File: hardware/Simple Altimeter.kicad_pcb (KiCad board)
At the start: 4 copper layers, 15.2 x 28.8 mm, 40 parts, among them J1 USB_C_Receptacle_USB2.0, J2 Conn_01x05_Pin, Q2 DMN3607LW, Q3 Q_NMOS_GDS, SW2 SW_Push, U1 WS4518, U2 BMP280, U3 W25Q16JVUXIQ, U4 STM32F042G6Ux, U5 XB6042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

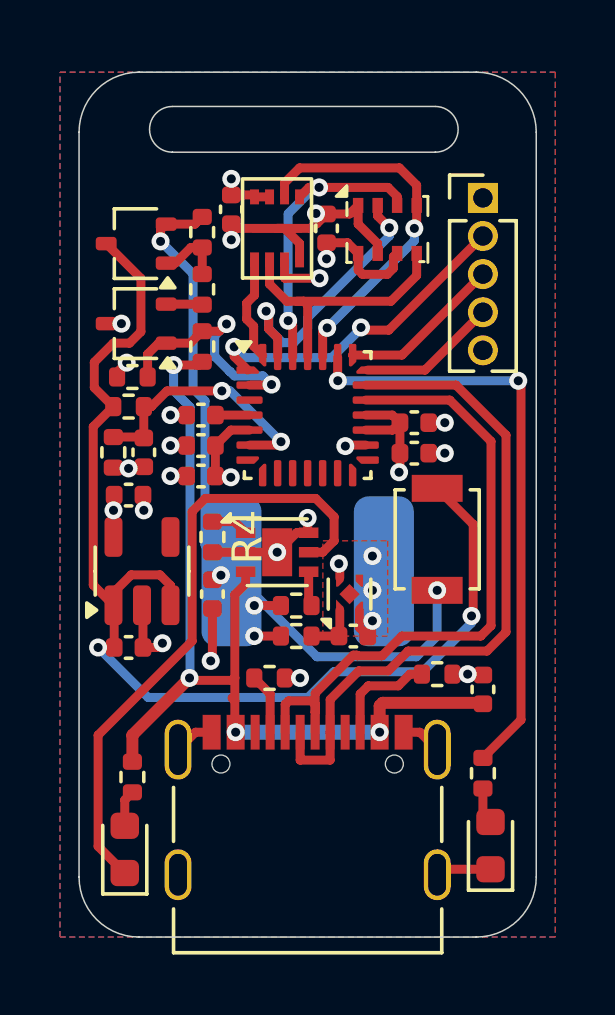
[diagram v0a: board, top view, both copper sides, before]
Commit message: Fixed boot pin and strengthened teather loop. Added BOMs and manufacturing data.
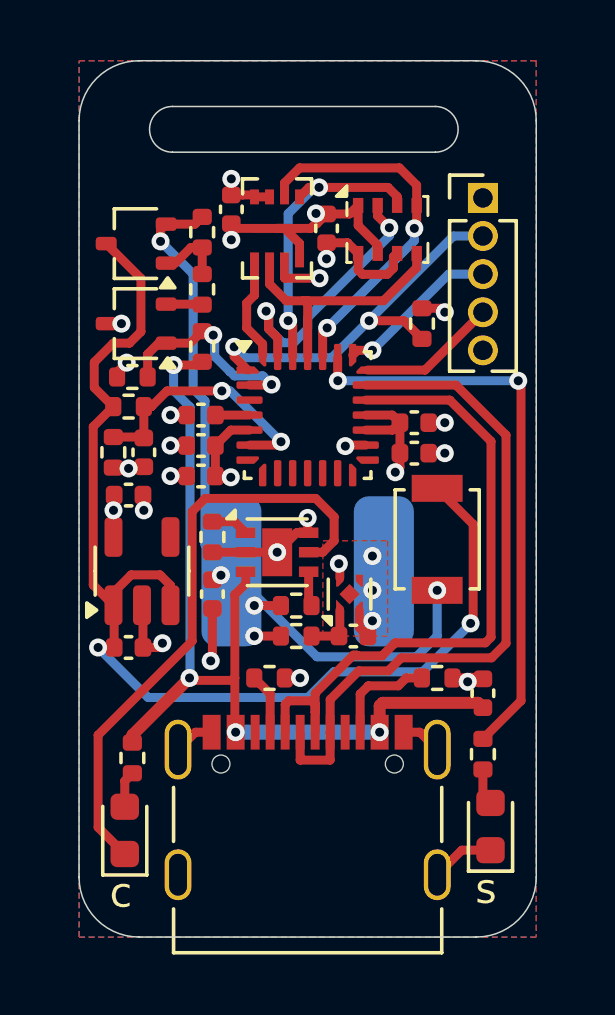
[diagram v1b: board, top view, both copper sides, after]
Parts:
- added R14: 33k3, Resistor_SMD:R_0402_1005Metric, F.Cu at (153.2, 105.8)
- D2: value LED -> RED LED
- moved R10 0.64 mm to (155.2, 120.1)
- moved D1 0.63 mm to (143.3, 122.7)
- moved D2 0.63 mm to (155.4, 122.6)
- moved R11 0.63 mm to (143.5, 120.3)
- moved R7 0.13 mm to (153.7, 117.6)
- moved C15 0.13 mm to (155.2, 118.1)
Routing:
- net /BATT-: track 3.78 -> 0.97 mm
- net /BOOT: track 11.2 -> 13.1 mm
- net /STAY_ALIVE: track 8.08 -> 7.07 mm
- net +5V: track 31.8 -> 30.8 mm
- net GND: track 28.9 -> 29.8 mm, vias 19 -> 20
- net Net-(D1-K): track 20.7 -> 20.1 mm
- net /LED: track 19.9 -> 19.3 mm
- net /SWDCLK: vias 0 -> 1
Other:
- board size 15.2 x 28.8 mm -> 15.2 x 29.2 mm
- board text added: "c"
- board text added: "s"

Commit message: Corrected Q1 schematic symbol (was NMOS, now correctly showing PMOS)
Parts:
- removed Q3: Q_NMOS_GDS, Package_TO_SOT_SMD:SOT-323_SC-70
- added Q1: DMP3099L, Package_TO_SOT_SMD:SOT-323_SC-70, F.Cu at (143.6, 103.1)
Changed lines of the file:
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@@
   (net 37 "Net-(Q2-D)")
   (net 38 "/STAY_ALIVE")
-  (net 39 "Net-(Q3-S)")
+  (net 39 "Net-(Q1-D)")
   (net 40 "/BOOT")
-  (net 41 "Net-(Q3-G)")
+  (net 41 "Net-(Q1-G)")
   (net 42 "unconnected-(U4-PA1-Pad7)")
   (net 43 "unconnected-(U4-PA2-Pad8)")
@@
       (stroke (width 0.1) (type solid)) (layer "F.Fab"))
     (pad "1" smd roundrect (at -0.51 0 270) (size 0.54 0.64) (layers "F.Cu" "F.Paste" "F.Mask") (roundrect_rratio 0.25)
-      (net 41 "Net-(Q3-G)") (pintype "passive"))
+      (net 41 "Net-(Q1-G)") (pintype "passive"))
     (pad "2" smd roundrect (at 0.51 0 270) (size 0.54 0.64) (layers "F.Cu" "F.Paste" "F.Mask") (roundrect_rratio 0.25)
       (net 37 "Net-(Q2-D)") (pintype "passive"))
@@
       (stroke (width 0.1) (type solid)) (layer "F.Fab"))
     (pad "1" smd roundrect (at -1.1375 -0.95 90) (size 1.325 0.6) (layers "F.Cu" "F.Paste" "F.Mask") (roundrect_rratio 0.25)
-      (net 39 "Net-(Q3-S)") (pinfunction "IN") (pintype "power_in"))
+      (net 39 "Net-(Q1-D)") (pinfunction "IN") (pintype "power_in"))
     (pad "2" smd roundrect (at -1.1375 0 90) (size 1.325 0.6) (layers "F.Cu" "F.Paste" "F.Mask") (roundrect_rratio 0.25)
       (net 2 "GND") (pinfunction "GND") (pintype "power_in"))
     (pad "3" smd roundrect (at -1.1375 0.95 90) (size 1.325 0.6) (layers "F.Cu" "F.Paste" "F.Mask") (roundrect_rratio 0.25)
-      (net 39 "Net-(Q3-S)") (pinfunction "EN") (pintype "input"))
+      (net 39 "Net-(Q1-D)") (pinfunction "EN") (pintype "input"))
     (pad "4" smd roundrect (at 1.1375 0.95 90) (size 1.325 0.6) (layers "F.Cu" "F.Paste" "F.Mask") (roundrect_rratio 0.25)
       (net 36 "unconnected-(U6-NC-Pad4)") (pinfunction "NC") (pintype "no_connect"))
@@
       (stroke (width 0.1) (type solid)) (fill none) (layer "F.Fab"))
     (pad "1" smd rect (at -1.7 0 270) (size 0.9 1.7) (layers "F.Cu" "F.Paste" "F.Mask")
-      (net 39 "Net-(Q3-S)") (pinfunction "1") (pintype "passive"))
+      (net 39 "Net-(Q1-D)") (pinfunction "1") (pintype "passive"))
     (pad "2" smd rect (at 1.7 0 270) (size 0.9 1.7) (layers "F.Cu" "F.Paste" "F.Mask")
       (net 24 "VBAT") (pinfunction "2") (pintype "passive"))
@@
       (stroke (width 0.1) (type solid)) (layer "F.Fab"))
     (pad "1" smd roundrect (at -0.48 0) (size 0.56 0.62) (layers "F.Cu" "F.Paste" "F.Mask") (roundrect_rratio 0.25)
-      (net 39 "Net-(Q3-S)") (pintype "passive"))
+      (net 39 "Net-(Q1-D)") (pintype "passive"))
     (pad "2" smd roundrect (at 0.48 0) (size 0.56 0.62) (layers "F.Cu" "F.Paste" "F.Mask") (roundrect_rratio 0.25)
       (net 2 "GND") (pintype "passive"))
@@
       (net 2 "GND") (pintype "passive"))
     (model "${KICAD6_3DMODEL_DIR}/Capacitor_SMD.3dshapes/C_0402_1005Metric.wrl"
-      (offset (xyz 0 0 0))
-      (scale (xyz 1 1 1))
-      (rotate (xyz 0 0 0))
-    )
-  )
-  (footprint "Package_TO_SOT_SMD:SOT-323_SC-70" (layer "F.Cu")
-    (at 143.637 103.124 180)
-    (descr "SOT-323, SC-70")
-    (tags "SOT-323 SC-70")
-    (property "Sheetfile" "Simple Altimeter.kicad_sch")
-    (property "Sheetname" "")
-    (property "ki_description" "N-MOSFET transistor, gate/drain/source")
-    (property "ki_keywords" "transistor NMOS N-MOS N-MOSFET")
-    (attr smd)
-    (fp_text reference "Q3" (at -0.05 -2.25) (layer "F.SilkS") hide
-        (effects (font (size 1 1) (thickness 0.15)))
-    )
-    (fp_text value "Q_NMOS_GDS" (at -0.05 2.05) (layer "F.Fab")
-        (effects (font (size 1 1) (thickness 0.15)))
-    )
-    (fp_text user "${REFERENCE}" (at 0 0 90) (layer "F.Fab")
-        (effects (font (size 0.5 0.5) (thickness 0.075)))
-    )
-    (fp_line (start -0.68 -1.16) (end 0.73 -1.16)
-      (stroke (width 0.12) (type solid)) (layer "F.SilkS"))
-    (fp_line (start -0.68 1.16) (end 0.73 1.16)
-      (stroke (width 0.12) (type solid)) (layer "F.SilkS"))
-    (fp_line (start 0.73 -1.16) (end 0.73 -0.5)
-      (stroke (width 0.12) (type solid)) (layer "F.SilkS"))
-    (fp_line (start 0.73 0.5) (end 0.73 1.16)
-      (stroke (width 0.12) (type solid)) (layer "F.SilkS"))
-    (fp_poly
-      (pts
-        (xy -1.05 -1.14)
-        (xy -1.29 -1.47)
-        (xy -0.81 -1.47)
-        (xy -1.05 -1.14)
-      )
-      (stroke (width 0.12) (type solid)) (fill solid) (layer "F.SilkS"))
-    (fp_line (start -1.7 -1.3) (end 1.7 -1.3)
-      (stroke (width 0.05) (type solid)) (layer "F.CrtYd"))
-    (fp_line (start -1.7 1.3) (end -1.7 -1.3)
-      (stroke (width 0.05) (type solid)) (layer "F.CrtYd"))
-    (fp_line (start 1.7 -1.3) (end 1.7 1.3)
-      (stroke (width 0.05) (type solid)) (layer "F.CrtYd"))
-    (fp_line (start 1.7 1.3) (end -1.7 1.3)
-      (stroke (width 0.05) (type solid)) (layer "F.CrtYd"))
-    (fp_line (start -0.68 -0.6) (end -0.68 1.1)
-      (stroke (width 0.1) (type solid)) (layer "F.Fab"))
-    (fp_line (start -0.18 -1.1) (end -0.68 -0.6)
-      (stroke (width 0.1) (type solid)) (layer "F.Fab"))
-    (fp_line (start 0.67 -1.1) (end -0.18 -1.1)
-      (stroke (width 0.1) (type solid)) (layer "F.Fab"))
-    (fp_line (start 0.67 -1.1) (end 0.67 1.1)
-      (stroke (width 0.1) (type solid)) (layer "F.Fab"))
-    (fp_line (start 0.67 1.1) (end -0.68 1.1)
-      (stroke (width 0.1) (type solid)) (layer "F.Fab"))
-    (pad "1" smd roundrect (at -1 -0.65 90) (size 0.45 0.7) (layers "F.Cu" "F.Paste" "F.Mask") (roundrect_rratio 0.25)
-      (net 41 "Net-(Q3-G)") (pinfunction "G") (pintype "input"))
-    (pad "2" smd roundrect (at -1 0.65 90) (size 0.45 0.7) (layers "F.Cu" "F.Paste" "F.Mask") (roundrect_rratio 0.25)
-      (net 24 "VBAT") (pinfunction "D") (pintype "passive"))
-    (pad "3" smd roundrect (at 1 0 90) (size 0.45 0.7) (layers "F.Cu" "F.Paste" "F.Mask") (roundrect_rratio 0.25)
-      (net 39 "Net-(Q3-S)") (pinfunction "S") (pintype "passive"))
-    (model "${KICAD6_3DMODEL_DIR}/Package_TO_SOT_SMD.3dshapes/SOT-323_SC-70.wrl"
       (offset (xyz 0 0 0))
       (scale (xyz 1 1 1))
@@
       (net 24 "VBAT") (pintype "passive"))
     (pad "2" smd roundrect (at 0.51 0 270) (size 0.54 0.64) (layers "F.Cu" "F.Paste" "F.Mask") (roundrect_rratio 0.25)
-      (net 41 "Net-(Q3-G)") (pintype "passive"))
+      (net 41 "Net-(Q1-G)") (pintype "passive"))
     (model "${KICAD6_3DMODEL_DIR}/Resistor_SMD.3dshapes/R_0402_1005Metric.wrl"
       (offset (xyz 0 0 0))
@@
       (stroke (width 0.1) (type solid)) (layer "F.Fab"))
     (pad "1" smd roundrect (at -0.51 0) (size 0.54 0.64) (layers "F.Cu" "F.Paste" "F.Mask") (roundrect_rratio 0.25)
-      (net 39 "Net-(Q3-S)") (pintype "passive"))
+      (net 39 "Net-(Q1-D)") (pintype "passive"))
     (pad "2" smd roundrect (at 0.51 0) (size 0.54 0.64) (layers "F.Cu" "F.Paste" "F.Mask") (roundrect_rratio 0.25)
       (net 4 "/BATT_SENSE") (pintype "passive"))
@@
       (offset (xyz 0 0 0))
       (scale (xyz 1 1 1))
+      (rotate (xyz 0 0 0))
+    )
+  )
+  (footprint "Package_TO_SOT_SMD:SOT-323_SC-70" (layer "F.Cu")
+    (at 143.637 103.124 180)
+    (descr "SOT-323, SC-70")
+    (tags "SOT-323 SC-70")
+    (property "Sheetfile" "Simple Altimeter.kicad_sch")
+    (property "Sheetname" "")
+    (property "ki_description" "P-MOSFET transistor, gate/source/drain")
+    (property "ki_keywords" "transistor PMOS P-MOS P-MOSFET")
+    (attr smd)
+    (fp_text reference "Q1" (at -0.05 -2.25) (layer "F.SilkS") hide
+        (effects (font (size 1 1) (thickness 0.15)))
+    )
+    (fp_text value "DMP3099L" (at -0.05 2.05) (layer "F.Fab")
+        (effects (font (size 1 1) (thickness 0.15)))
+    )
+    (fp_text user "${REFERENCE}" (at 0 0 90) (layer "F.Fab")
+        (effects (font (size 0.5 0.5) (thickness 0.075)))
+    )
+    (fp_line (start -0.68 -1.16) (end 0.73 -1.16)
+      (stroke (width 0.12) (type solid)) (layer "F.SilkS"))
+    (fp_line (start -0.68 1.16) (end 0.73 1.16)
+      (stroke (width 0.12) (type solid)) (layer "F.SilkS"))
+    (fp_line (start 0.73 -1.16) (end 0.73 -0.5)
+      (stroke (width 0.12) (type solid)) (layer "F.SilkS"))
+    (fp_line (start 0.73 0.5) (end 0.73 1.16)
+      (stroke (width 0.12) (type solid)) (layer "F.SilkS"))
+    (fp_poly
+      (pts
+        (xy -1.05 -1.14)
+        (xy -1.29 -1.47)
+        (xy -0.81 -1.47)
+        (xy -1.05 -1.14)
+      )
+      (stroke (width 0.12) (type solid)) (fill solid) (layer "F.SilkS"))
+    (fp_line (start -1.7 -1.3) (end 1.7 -1.3)
+      (stroke (width 0.05) (type solid)) (layer "F.CrtYd"))
+    (fp_line (start -1.7 1.3) (end -1.7 -1.3)
+      (stroke (width 0.05) (type solid)) (layer "F.CrtYd"))
+    (fp_line (start 1.7 -1.3) (end 1.7 1.3)
+      (stroke (width 0.05) (type solid)) (layer "F.CrtYd"))
+    (fp_line (start 1.7 1.3) (end -1.7 1.3)
+      (stroke (width 0.05) (type solid)) (layer "F.CrtYd"))
+    (fp_line (start -0.68 -0.6) (end -0.68 1.1)
+      (stroke (width 0.1) (type solid)) (layer "F.Fab"))
+    (fp_line (start -0.18 -1.1) (end -0.68 -0.6)
+      (stroke (width 0.1) (type solid)) (layer "F.Fab"))
+    (fp_line (start 0.67 -1.1) (end -0.18 -1.1)
+      (stroke (width 0.1) (type solid)) (layer "F.Fab"))
+    (fp_line (start 0.67 -1.1) (end 0.67 1.1)
+      (stroke (width 0.1) (type solid)) (layer "F.Fab"))
+    (fp_line (start 0.67 1.1) (end -0.68 1.1)
+      (stroke (width 0.1) (type solid)) (layer "F.Fab"))
+    (pad "1" smd roundrect (at -1 -0.65 90) (size 0.45 0.7) (layers "F.Cu" "F.Paste" "F.Mask") (roundrect_rratio 0.25)
+      (net 41 "Net-(Q1-G)") (pinfunction "G") (pintype "input"))
+    (pad "2" smd roundrect (at -1 0.65 90) (size 0.45 0.7) (layers "F.Cu" "F.Paste" "F.Mask") (roundrect_rratio 0.25)
+      (net 24 "VBAT") (pinfunction "S") (pintype "passive"))
+    (pad "3" smd roundrect (at 1 0 90) (size 0.45 0.7) (layers "F.Cu" "F.Paste" "F.Mask") (roundrect_rratio 0.25)
+      (net 39 "Net-(Q1-D)") (pinfunction "D") (pintype "passive"))
+    (model "${KICAD6_3DMODEL_DIR}/Package_TO_SOT_SMD.3dshapes/SOT-323_SC-70.wrl"
+      (offset (xyz 0 0 0))
+      (scale (xyz 1 1 1))

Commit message: updated button part number
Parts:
- Q1: value DMP3099L -> DMP2240UW
- Q2: value DMN3607LW -> DMN3067LW
- SW1: renamed from SW2; value SW_Push -> B3U-1000P
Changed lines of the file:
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@@
         (effects (font (size 1 1) (thickness 0.15)))
     )
-    (fp_text value "DMN3607LW" (at -0.05 2.05) (layer "F.Fab")
+    (fp_text value "DMN3067LW" (at -0.05 2.05) (layer "F.Fab")
         (effects (font (size 1 1) (thickness 0.15)))
     )
@@
     (property "ki_keywords" "switch normally-open pushbutton push-button")
     (attr smd)
-    (fp_text reference "SW2" (at 0 -2.5 90) (layer "F.SilkS") hide
-        (effects (font (size 1 1) (thickness 0.15)))
-    )
-    (fp_text value "SW_Push" (at 0 2.5 90) (layer "F.Fab")
+    (fp_text reference "SW1" (at 0 -2.5 90) (layer "F.SilkS") hide
+        (effects (font (size 1 1) (thickness 0.15)))
+    )
+    (fp_text value "B3U-1000P" (at 0 2.5 90) (layer "F.Fab")
         (effects (font (size 1 1) (thickness 0.15)))
     )
@@
         (effects (font (size 1 1) (thickness 0.15)))
     )
-    (fp_text value "DMP3099L" (at -0.05 2.05) (layer "F.Fab")
-        (effects (font (size 1 1) (thickness 0.15)))
-    )
+    (fp_text value "DMP2240UW" (at -0.05 2.05) (layer "F.Fab")
+        (effects (font (size 1 1) (thickness 0.15)))
+    )

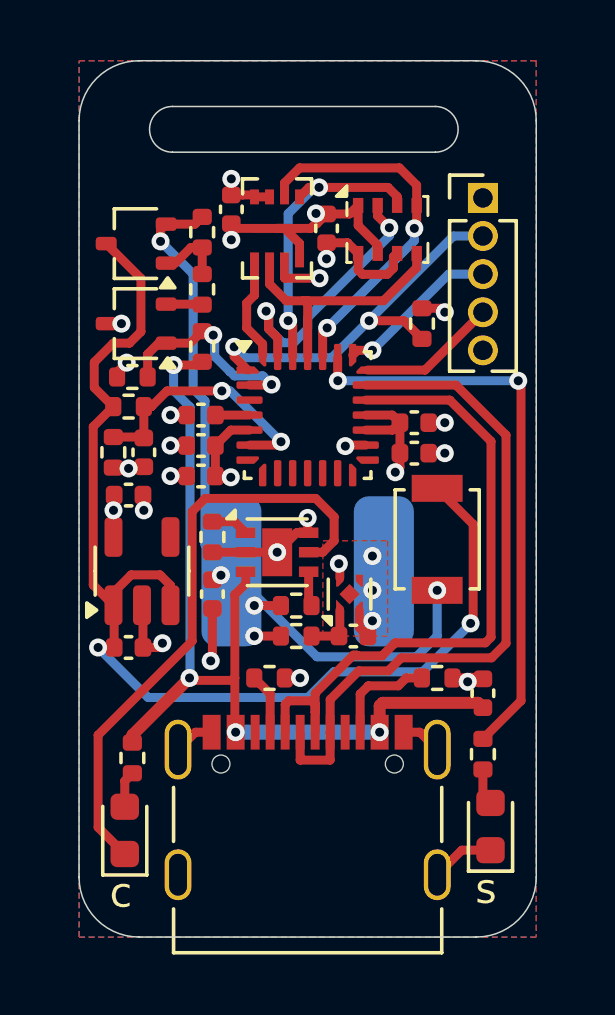
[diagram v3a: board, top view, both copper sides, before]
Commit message: Adding operation.md
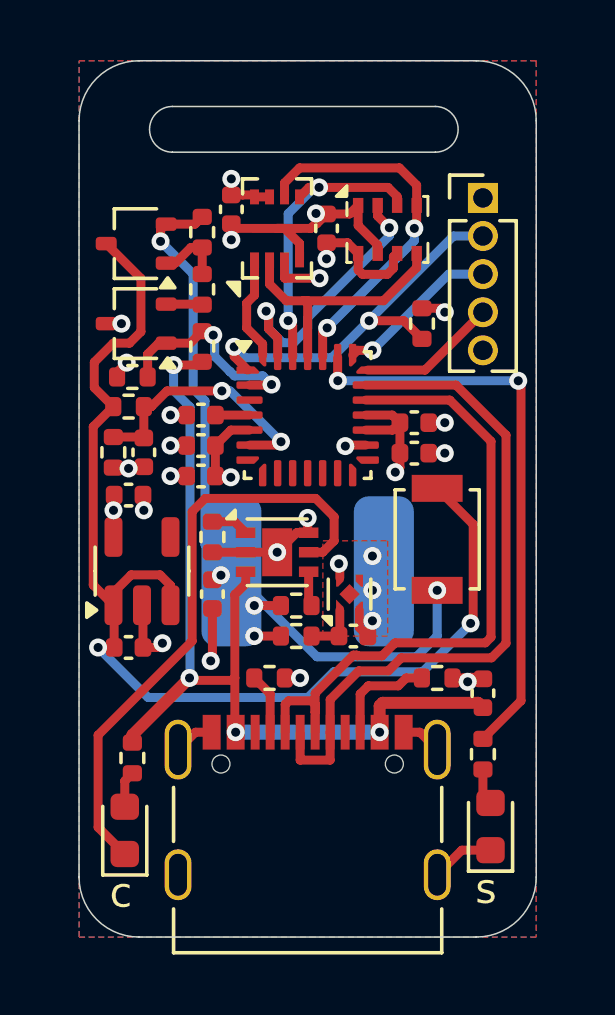
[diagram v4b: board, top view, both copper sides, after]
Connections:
- U6 pad 4: unconnected-(U6-NC-Pad4) -> GND
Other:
- board text added: "SimpleAlt Rev2"

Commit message: Initial commit of STNS01 fork. This will probably become main at some stage in the future.
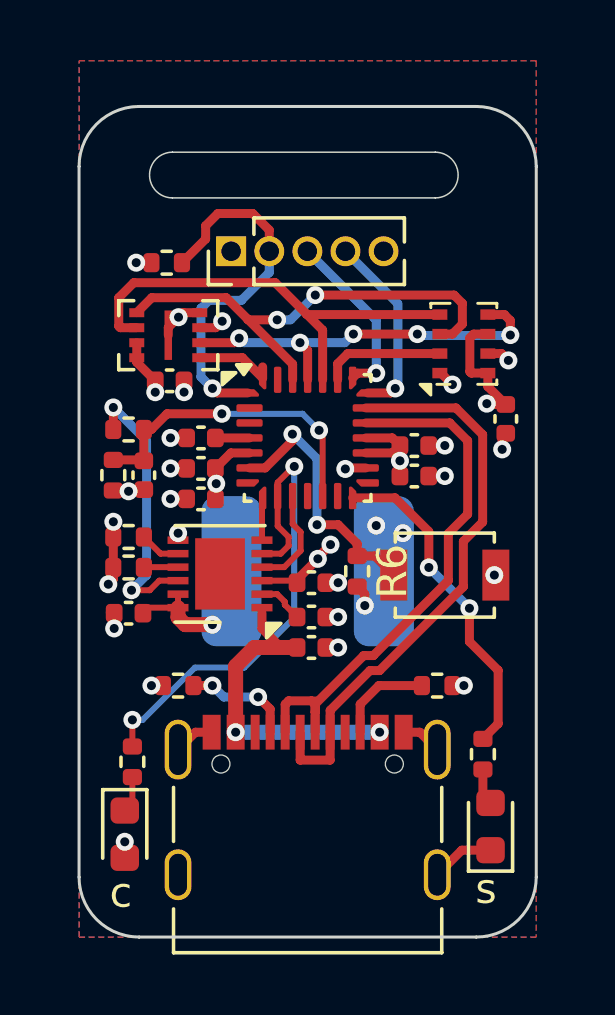
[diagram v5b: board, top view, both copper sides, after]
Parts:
- removed C15: 1u, Capacitor_SMD:C_0402_1005Metric
- removed Q1: DMP2240UW, Package_TO_SOT_SMD:SOT-323_SC-70
- removed Q2: DMN3067LW, Package_TO_SOT_SMD:SOT-323_SC-70
- removed R11: 1k, Resistor_SMD:R_0402_1005Metric
- removed R12, R13, R9: 33k3, Resistor_SMD:R_0402_1005Metric
- removed U1: WS4518, Package_DFN_QFN:DFN-6-1EP_2x2mm_P0.65mm_EP1x1.6mm
- removed U5: XB6042, Package_DFN_QFN:UDFN-4-1EP_1x1mm_P0.65mm_EP0.48x0.48mm
- removed U6: TLV75533PDBV, Package_TO_SOT_SMD:SOT-23-5
- added U7: ~, Package_DFN_QFN:DFN-12-1EP_3x3mm_P0.45mm_EP1.66x2.38mm, F.Cu at (146.4, 114.1)
- C1, C3: value 1u -> 4u7
- C7: value 4u7 -> 1u
- D1: value AMBER LED -> RED LED
- R3: value 1k -> 5k1
- R4: value 33k3 -> 10k
- R5: value 1R -> 1k
- SW1: value B3U-1000P -> SW_Push
- moved R3 9.59 mm to (143.4, 113.9), turned to 180 degrees
- moved R14 8.75 mm to (144.7, 103.8), turned to 180 degrees
- moved C5 8.72 mm to (156.0, 109.0), turned to -90 degrees
- moved J2 8.58 mm to (146.8, 103.4), turned to 90 degrees
- moved R5 7.55 mm to (143.5, 120.4), turned to 90 degrees
- moved C1 6.18 mm to (149.5, 115.6)
- moved C13 6.07 mm to (144.8, 107.7), turned to 0 degrees
- moved U3 5.08 mm to (144.7, 106.2), turned to 180 degrees
- moved U2 4.59 mm to (154.6, 106.5), turned to 90 degrees
- moved C3 3.94 mm to (143.4, 115.4), turned to 180 degrees
- moved C7 3.75 mm to (149.5, 116.6), turned to 0 degrees
- moved R8 3.06 mm to (145.0, 117.9), turned to 180 degrees
- moved R6 2.96 mm to (151.0, 114.0), turned to -90 degrees
- moved R4 2.79 mm to (143.4, 112.9), turned to 180 degrees
- moved C11 2.26 mm to (149.5, 114.4)
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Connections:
- BT1 pad 1: VBAT -> Net-(BT1-+)
- BT1 pad 2: /BATT- -> GND
- C1 pad 1: Net-(Q1-D) -> Net-(U7-LDO)
- C11 pad 1: Net-(U5-VDD) -> +3.3V
- C11 pad 2: /BATT- -> GND
- C3 pad 1: +3.3V -> Net-(BT1-+)
- C7 pad 1: VBAT -> +5V
- D1 pad 2: Net-(D1-A) -> +3.3V
- R1 pad 1: Net-(Q1-D) -> Net-(U7-BATMS)
- R3 pad 2: Net-(Q2-D) -> GND
- R5 pad 1: Net-(U1-BAT) -> Net-(D1-K)
- R5 pad 2: VBAT -> /~{CHARGE}
- R6 pad 1: VBAT -> /BUTTON
- R6 pad 2: Net-(U5-VDD) -> GND
- SW1 pad 1: Net-(Q1-D) -> /BUTTON
- SW1 pad 2: VBAT -> +3.3V
- U4 pad 10: unconnected-(U4-PA4-Pad10) -> /SHUTDOWN
- U4 pad 12: unconnected-(U4-PA6-Pad12) -> /BATT_SENSE
- U4 pad 14: unconnected-(U4-PB0-Pad14) -> /LED
- U4 pad 2: /STAY_ALIVE -> unconnected-(U4-PF0-Pad2)
- U4 pad 23: /LED -> /BMP_~{CS}
- U4 pad 27: /BMP_~{CS} -> unconnected-(U4-PB6-Pad27)
- U4 pad 6: /BATT_SENSE -> /BUTTON
- U4 pad 8: unconnected-(U4-PA2-Pad8) -> /CHARGE_EN
- U4 pad 9: unconnected-(U4-PA3-Pad9) -> /~{CHARGE}
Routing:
- net Net-(Q1-D): track 38.4 -> 0.00 mm, vias 2 -> 0
- net VBAT: track 25.8 -> 0.00 mm, vias 5 -> 0
- net +5V: track 30.8 -> 11.4 mm, vias 4 -> 2
- net Net-(D1-K): track 20.1 -> 1.22 mm
- net /~{CHARGE}: track 0.00 -> 16.8 mm, vias 0 -> 2
- net GND: track 29.8 -> 19.3 mm, vias 20 -> 25
- net Net-(U7-BATMS): track 0.00 -> 9.18 mm, vias 0 -> 2
- net /BUTTON: track 0.00 -> 8.88 mm, vias 0 -> 2
- net /LED: track 19.3 -> 11.1 mm
- net /STAY_ALIVE: track 7.07 -> 0.00 mm, vias 2 -> 0
- net /MOSI: track 10.0 -> 16.1 mm
- net /BMP_~{CS}: track 9.39 -> 4.08 mm, vias 2 -> 0
- net /MISO: track 8.75 -> 13.3 mm, vias 0 -> 5
- net /USB_P: track 22.9 -> 19.3 mm
- net /USB_N: track 21.5 -> 18.1 mm
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- removed copper zone on F.Cu, net /BATT-
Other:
- board size 15.2 x 29.2 mm -> 15.2 x 27.7 mm
- board text added: "(C) 2024 Michael Turner"
- board text added: "YAY ROCKETS!"
